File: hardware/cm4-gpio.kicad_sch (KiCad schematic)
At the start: 6 parts, among them J2 DF40C-100DP-0.4V_51_

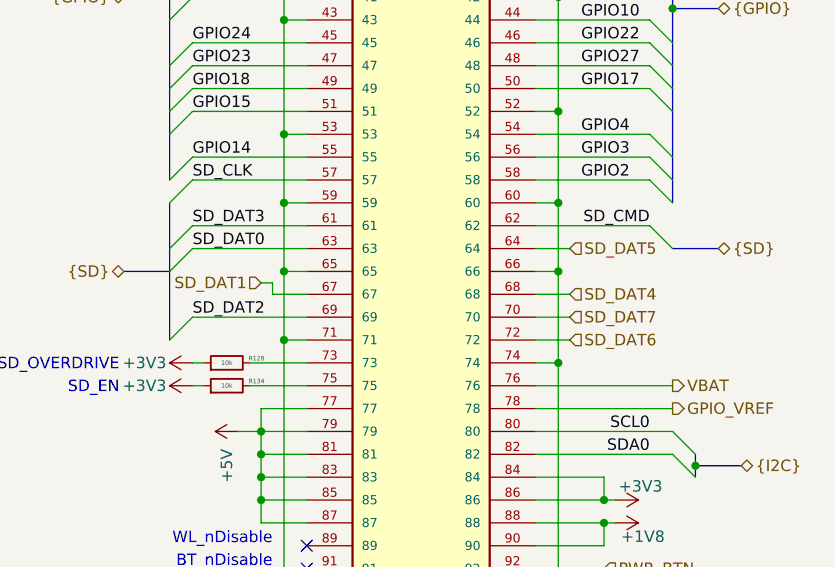
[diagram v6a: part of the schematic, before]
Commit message: Routing BTNs, LEDs, CLK
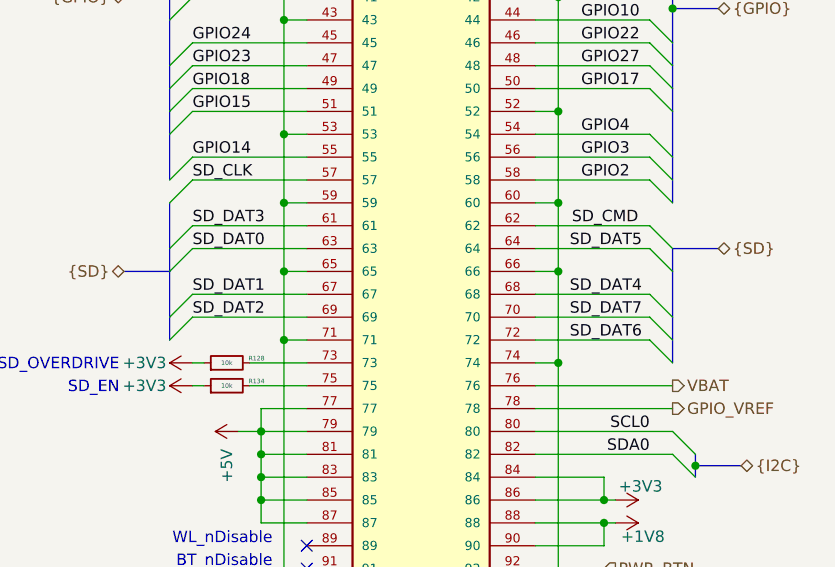
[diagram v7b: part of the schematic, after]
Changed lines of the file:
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@@
 	)
 	(bus_alias "I2C"
-		(members "SCL0" "SDA0")
+		(members "SCL0" "SDA0" "ID_SC" "ID_SD")
 	)
 	(bus_alias "SD"
@@
 	)
 	(bus_entry
+		(at 259.08 113.03)
+		(size 2.54 2.54)
+		(stroke
+			(width 0)
+			(type default)
+		)
+	)
+	(bus_entry
 		(at 259.08 59.69)
 		(size 2.54 2.54)
@@
 	)
 	(bus_entry
+		(at 259.08 115.57)
+		(size 2.54 2.54)
+		(stroke
+			(width 0)
+			(type default)
+		)
+	)
+	(bus_entry
 		(at 259.08 57.15)
 		(size 2.54 2.54)
@@
 	)
 	(bus_entry
+		(at 259.08 105.41)
+		(size 2.54 2.54)
+		(stroke
+			(width 0)
+			(type default)
+		)
+	)
+	(bus_entry
 		(at 259.08 31.75)
 		(size 2.54 2.54)
@@
 	)
 	(bus_entry
+		(at 208.28 110.49)
+		(size -2.54 2.54)
+		(stroke
+			(width 0)
+			(type default)
+		)
+	)
+	(bus_entry
+		(at 259.08 110.49)
+		(size 2.54 2.54)
+		(stroke
+			(width 0)
+			(type default)
+		)
+	)
+	(bus_entry
 		(at 208.28 64.77)
 		(size -2.54 2.54)
@@
 		)
 	)
+	(bus
+		(pts
+			(xy 261.62 105.41) (xy 261.62 107.95)
+		)
+		(stroke
+			(width 0)
+			(type default)
+		)
+	)
 	(wire
 		(pts
@@
 	(wire
 		(pts
-			(xy 246.38 110.49) (xy 250.19 110.49)
+			(xy 246.38 110.49) (xy 259.08 110.49)
 		)
 		(stroke
@@
 	(wire
 		(pts
-			(xy 246.38 115.57) (xy 250.19 115.57)
+			(xy 246.38 115.57) (xy 259.08 115.57)
 		)
 		(stroke
@@
 		)
 	)
+	(bus
+		(pts
+			(xy 205.74 113.03) (xy 205.74 115.57)
+		)
+		(stroke
+			(width 0)
+			(type default)
+		)
+	)
 	(wire
 		(pts
@@
 	(wire
 		(pts
-			(xy 217.17 109.22) (xy 217.17 110.49)
-		)
-		(stroke
-			(width 0)
-			(type default)
-		)
-	)
-	(wire
-		(pts
 			(xy 246.38 90.17) (xy 248.92 90.17)
 		)
@@
 	(wire
 		(pts
-			(xy 246.38 113.03) (xy 250.19 113.03)
+			(xy 246.38 113.03) (xy 259.08 113.03)
 		)
 		(stroke
@@
 		)
 	)
+	(bus
+		(pts
+			(xy 261.62 115.57) (xy 261.62 118.11)
+		)
+		(stroke
+			(width 0)
+			(type default)
+		)
+	)
 	(wire
 		(pts
@@
 		)
 	)
+	(bus
+		(pts
+			(xy 261.62 107.95) (xy 261.62 113.03)
+		)
+		(stroke
+			(width 0)
+			(type default)
+		)
+	)
 	(wire
 		(pts
@@
 	(wire
 		(pts
-			(xy 217.17 110.49) (xy 220.98 110.49)
-		)
-		(stroke
-			(width 0)
-			(type default)
-		)
-	)
-	(wire
-		(pts
 			(xy 218.44 54.61) (xy 218.44 67.31)
 		)
@@
 	(wire
 		(pts
-			(xy 215.9 109.22) (xy 217.17 109.22)
-		)
-		(stroke
-			(width 0)
-			(type default)
-		)
-	)
-	(wire
-		(pts
 			(xy 208.28 46.99) (xy 220.98 46.99)
 		)
@@
 	(bus
 		(pts
-			(xy 205.74 107.95) (xy 205.74 115.57)
+			(xy 205.74 107.95) (xy 205.74 113.03)
 		)
 		(stroke
@@
 	(wire
 		(pts
-			(xy 246.38 105.41) (xy 250.19 105.41)
+			(xy 246.38 105.41) (xy 259.08 105.41)
 		)
 		(stroke
@@
 	(bus
 		(pts
+			(xy 261.62 113.03) (xy 261.62 115.57)
+		)
+		(stroke
+			(width 0)
+			(type default)
+		)
+	)
+	(bus
+		(pts
 			(xy 205.74 31.75) (xy 205.74 34.29)
 		)
@@
 		(pts
 			(xy 205.74 67.31) (xy 205.74 74.93)
+		)
+		(stroke
+			(width 0)
+			(type default)
+		)
+	)
+	(wire
+		(pts
+			(xy 208.28 110.49) (xy 220.98 110.49)
 		)
 		(stroke
@@
 		)
 	)
+	(label "SD_DAT4"
+		(at 250.19 110.49 0)
+		(effects
+			(font
+				(size 1.27 1.27)
+			)
+			(justify left bottom)
+		)
+	)
 	(label "GPIO12"
 		(at 208.28 64.77 0)
@@
 		)
 	)
+	(label "SD_DAT7"
+		(at 250.19 113.03 0)
+		(effects
+			(font
+				(size 1.27 1.27)
+			)
+			(justify left bottom)
+		)
+	)
 	(label "ETH3_N"
 		(at 208.28 31.75 0)
@@
 	)
 	(label "SD_CMD"
-		(at 259.08 102.87 180)
+		(at 257.81 102.87 180)
 		(effects
 			(font
@@
 		)
 	)
+	(label "SD_DAT5"
+		(at 250.19 105.41 0)
+		(effects
+			(font
+				(size 1.27 1.27)
+			)
+			(justify left bottom)
+		)
+	)
 	(label "GPIO2"
 		(at 251.46 97.79 0)
@@
 		)
 	)
+	(label "SD_DAT6"
+		(at 250.19 115.57 0)
+		(effects
+			(font
+				(size 1.27 1.27)
+			)
+			(justify left bottom)
+		)
+	)
 	(label "GPIO24"
 		(at 208.28 82.55 0)
@@
 		)
 	)
+	(label "SD_DAT1"
+		(at 208.28 110.49 0)
+		(effects
+			(font
+				(size 1.27 1.27)
+			)
+			(justify left bottom)
+		)
+	)
 	(label "ETH2_P"
 		(at 208.28 39.37 0)
@@
 			)
 			(justify left bottom)
-		)
-	)
-	(hierarchical_label "SD_DAT5"
-		(shape input)
-		(at 250.19 105.41 0)
-		(effects
-			(font
-				(size 1.27 1.27)
-			)
-			(justify left)
 		)
 	)
@@
 		)
 	)
-	(hierarchical_label "SD_DAT4"
-		(shape input)
-		(at 250.19 110.49 0)
-		(effects
-			(font
-				(size 1.27 1.27)
-			)
-			(justify left)
-		)
-	)
 	(hierarchical_label "{GPIO}"
 		(shape bidirectional)
@@
 		)
 	)
-	(hierarchical_label "SD_DAT7"
-		(shape input)
-		(at 250.19 113.03 0)
-		(effects
-			(font
-				(size 1.27 1.27)
-			)
-			(justify left)
-		)
-	)
 	(hierarchical_label "{SD}"
 		(shape bidirectional)
@@
 		)
 	)
-	(hierarchical_label "SD_DAT6"
-		(shape input)
-		(at 250.19 115.57 0)
-		(effects
-			(font
-				(size 1.27 1.27)
-			)
-			(justify left)
-		)
-	)
 	(hierarchical_label "nLED_act"
 		(shape input)
@@
 		(effects
 			(font
-				(size 1.27 1.27)
-			)
-			(justify right)
-		)
-	)
-	(hierarchical_label "SD_DAT1"
-		(shape input)
-		(at 215.9 109.22 180)
-		(effects
-			(font

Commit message: Routing
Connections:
- net USB_CC1: no longer J2.94
- net USB_CC2: no longer J2.96
- no-connect marks 2 -> 6
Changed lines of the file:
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@@
+	)
+	(no_connect
+		(at 254 143.51)
+	)
+	(no_connect
+		(at 261.62 143.51)
 	)
 	(no_connect
 		(at 220.98 138.43)
+	)
+	(no_connect
+		(at 254 146.05)
+	)
+	(no_connect
+		(at 261.62 146.05)
 	)
 	(no_connect
@@
 	(hierarchical_label "USB_CC2"
 		(shape passive)
-		(at 254 146.05 0)
+		(at 261.62 146.05 0)
 		(effects
 			(font
@@
 	(hierarchical_label "USB_CC1"
 		(shape passive)
-		(at 254 143.51 0)
-		(effects
-			(font
+		(at 261.62 143.51 0)
+		(effects
+			(font
